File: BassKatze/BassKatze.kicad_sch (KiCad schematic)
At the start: 42 parts, among them U1 ESP32-WROOM-32D

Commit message: esp32 version
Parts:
- added C3: 100nF, Capacitor_SMD:C_0603_1608Metric, symbol Device:C
- added JP1: Jumper_2_Bridged, Jumper:SolderJumper-2_P1.3mm_Bridged_RoundedPad1.0x1.5mm, symbol Jumper:Jumper_2_Bridged
- added Q1, Q2: N-channel 30V 5A, Package_TO_SOT_SMD:SOT-23, symbol ESP32-DEVKITC-32D:SL2300
- added R4: 20k?, Resistor_SMD:R_0603_1608Metric, symbol Device:R
- added R6: 100Ohm, Resistor_SMD:R_0603_1608Metric, symbol Device:R
- added U2: hy2112, Package_TO_SOT_SMD:SOT-23-6_Handsoldering, symbol hy2112:hy2112
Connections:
- net 3V3: now also R6.2
- net Attack_Select: now also U1.8 (IO32); no longer U1.7 (IO35)
- net GND: now also JP1.2 (B), Q2.2 (S); no longer BAT-1.1 (Pin_1), BAT-2.1 (Pin_1)
- net MIC: now also U1.7 (IO35); no longer U1.8 (IO32)
- new net: JP1.1 (A), Q1.3 (D), Q2.3 (D), R4.2
- new net: Q2.1 (G), U2.3 (OC)
- new net: Q1.1 (G), U2.1 (OD)
- new net: R4.1, U2.2 (CS)
- new net: C3.1, R6.1, U2.5 (VDD)
- new net BAT-: BAT-1.1 (Pin_1), BAT-2.1 (Pin_1), C3.2, Q1.2 (S), U2.6 (VSS)

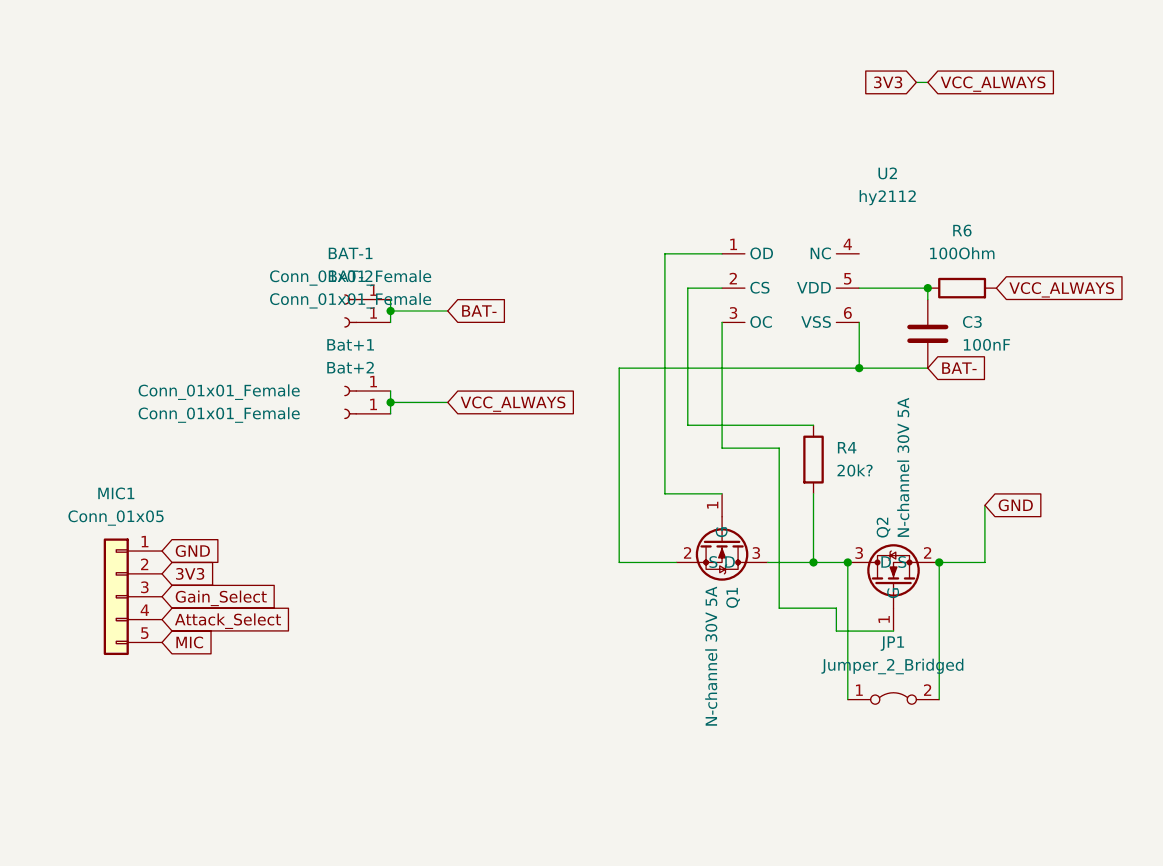
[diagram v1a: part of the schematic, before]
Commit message: use hardware dma
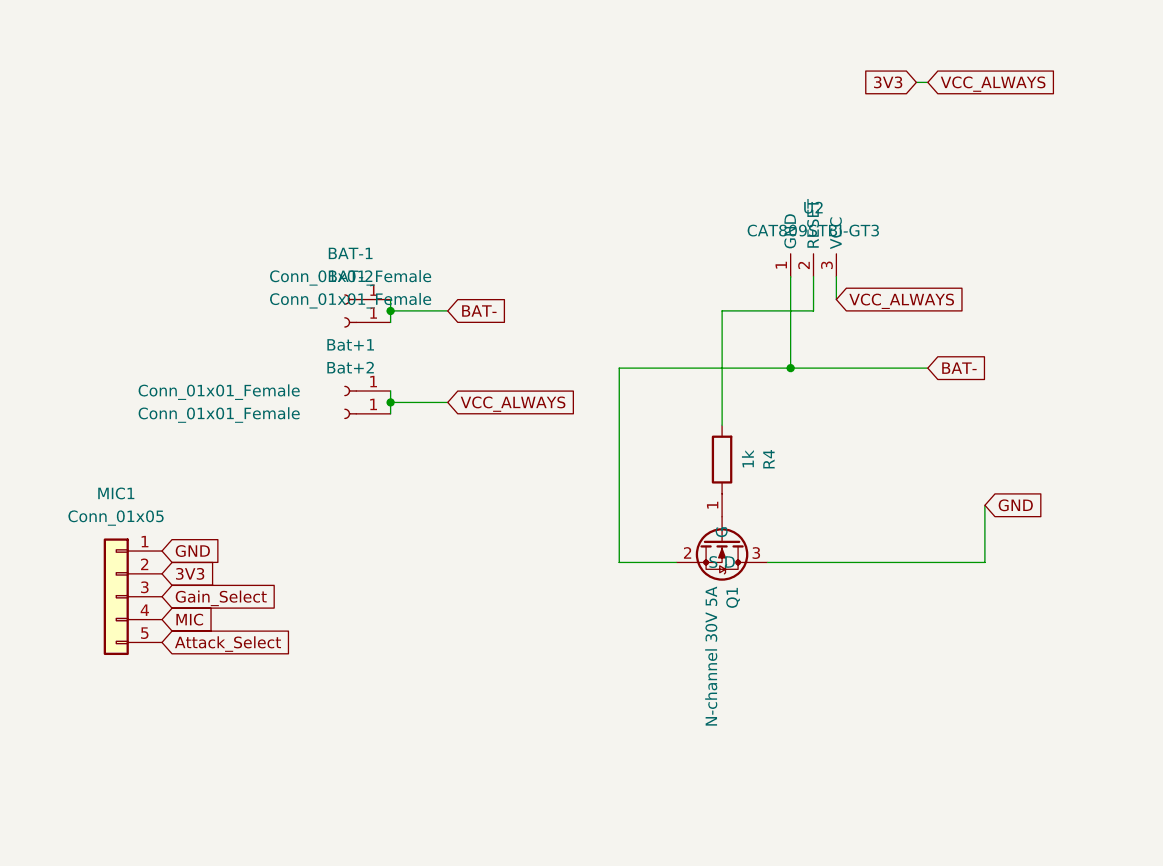
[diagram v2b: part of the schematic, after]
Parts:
- removed C3: 100nF, Capacitor_SMD:C_0603_1608Metric, symbol Device:C
- removed JP1: Jumper_2_Bridged, Jumper:SolderJumper-2_P1.3mm_Bridged_RoundedPad1.0x1.5mm, symbol Jumper:Jumper_2_Bridged
- removed Q2: N-channel 30V 5A, Package_TO_SOT_SMD:SOT-23, symbol ESP32-DEVKITC-32D:SL2300
- removed R6: 100Ohm, Resistor_SMD:R_0603_1608Metric, symbol Device:R
- removed U2: hy2112, Package_TO_SOT_SMD:SOT-23-6_Handsoldering, symbol hy2112:hy2112
- added U2: CAT809STBI-GT3, Package_TO_SOT_SMD:SOT-23, symbol hy2112:AP0809
- BAT-1, BAT-2, Bat+1, Bat+2: footprint Connector_Wire:SolderWirePad_1x01_SMD_1x2mm -> Connector_Wire:SolderWirePad_1x01_SMD_5x10mm
- R4: value 20k? -> 1k; LCSC (none) -> C21190
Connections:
- net 3V3: now also U2.3 (VCC)
- net Attack_Select: now also MIC1.5 (Pin_5); no longer MIC1.4 (Pin_4)
- net BAT-: now also U2.1 (GND)
- net GND: now also Q1.3 (D)
- net MIC: now also MIC1.4 (Pin_4); no longer MIC1.5 (Pin_5)
- net at R4.2: now also U2.2 (RESET); no longer Q1.3 (D)
- net at Q1.1 (G): now also R4.1
